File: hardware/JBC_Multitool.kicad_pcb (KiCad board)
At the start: 2 copper layers, 122 x 93 mm, 46 parts, among them J1 Screw_Terminal_01x02, J4 Mini XLR6, J5 Mini XLR6, J6 Binder 09-0998-00-05, J7 Binder 09-0998-00-05, K1 RT314005, K10 HF49FD_005-1H12T, K11 HF49FD_005-1H12T, K2 HF49FD_005-1H12T, K3 HF49FD_005-1H12T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

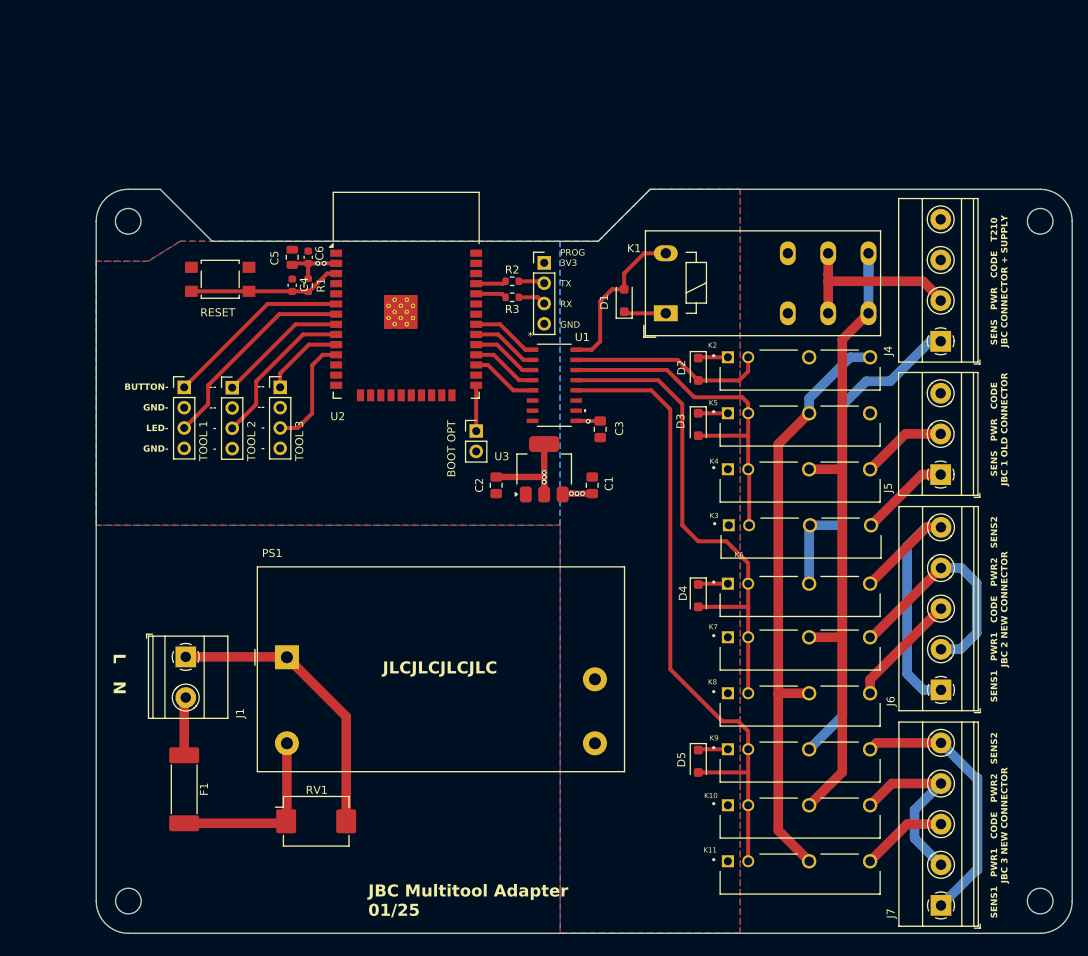
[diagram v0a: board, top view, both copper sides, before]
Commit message: corrected pin numbers on terminal footprint, changed switch-LED configuration
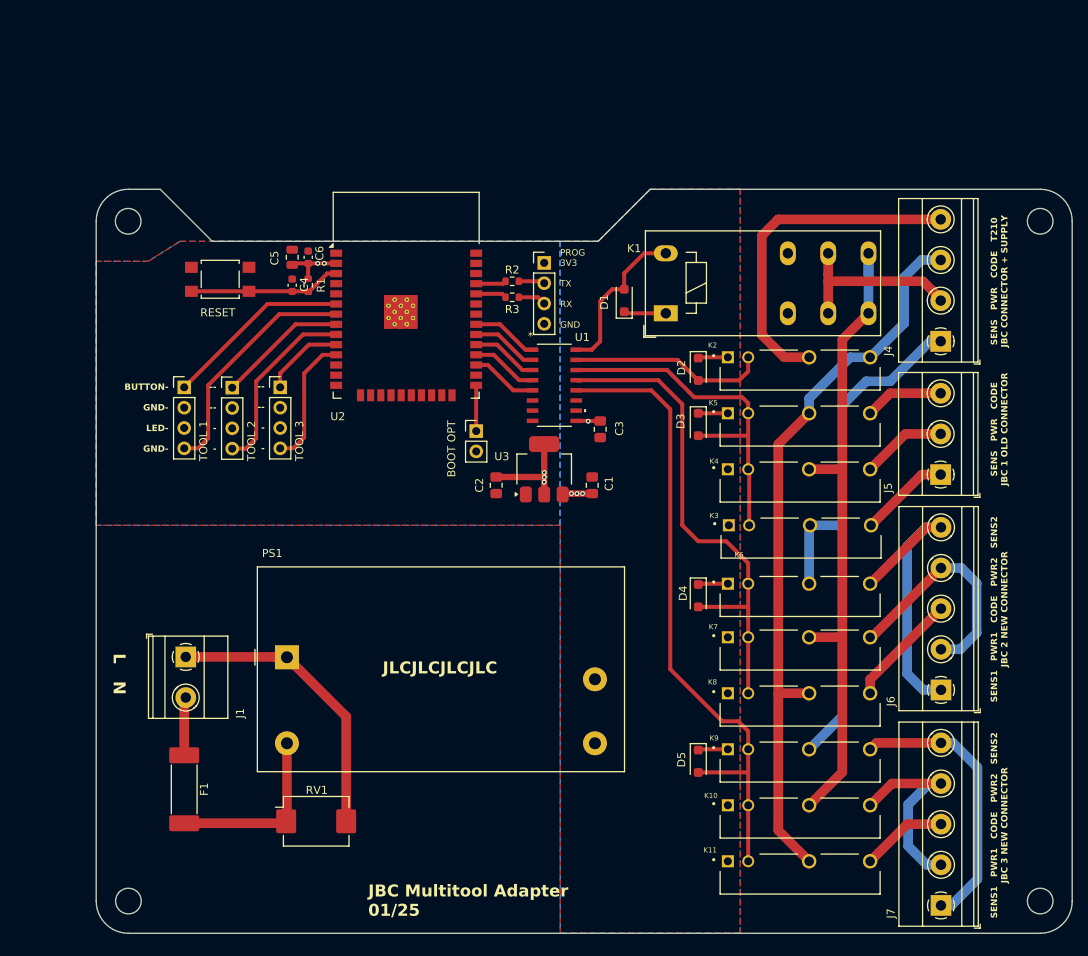
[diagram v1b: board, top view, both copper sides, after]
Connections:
- SELECT_TOOL_1 pad 3: /SELECT_TOOL_LED_1 -> +3.3V
- SELECT_TOOL_1 pad 4: GND -> /SELECT_TOOL_LED_1
- SELECT_TOOL_2 pad 3: /SELECT_TOOL_LED_2 -> +3.3V
- SELECT_TOOL_2 pad 4: GND -> /SELECT_TOOL_LED_2
- SELECT_TOOL_3 pad 3: /SELECT_TOOL_LED_3 -> +3.3V
- SELECT_TOOL_3 pad 4: GND -> /SELECT_TOOL_LED_3
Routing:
- net /RELAIS_CARD/T210_TOOL_CODE: track 0.00 -> 42.7 mm
- net /RELAIS_CARD/TOOL_CODE: track 74.7 -> 91.9 mm
- net Net-(J5-P5): track 0.00 -> 9.86 mm
- net /SELECT_TOOL_LED_1: track 26.3 -> 29.8 mm
- net /SELECT_TOOL_LED_2: track 19.5 -> 23.1 mm
- net Net-(J7-P2): track 23.7 -> 26.2 mm
- net /SELECT_TOOL_LED_3: track 14.3 -> 16.5 mm
- net Net-(J7-P1): track 33.5 -> 34.9 mm

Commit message: added 2.nd "old" jbc connector
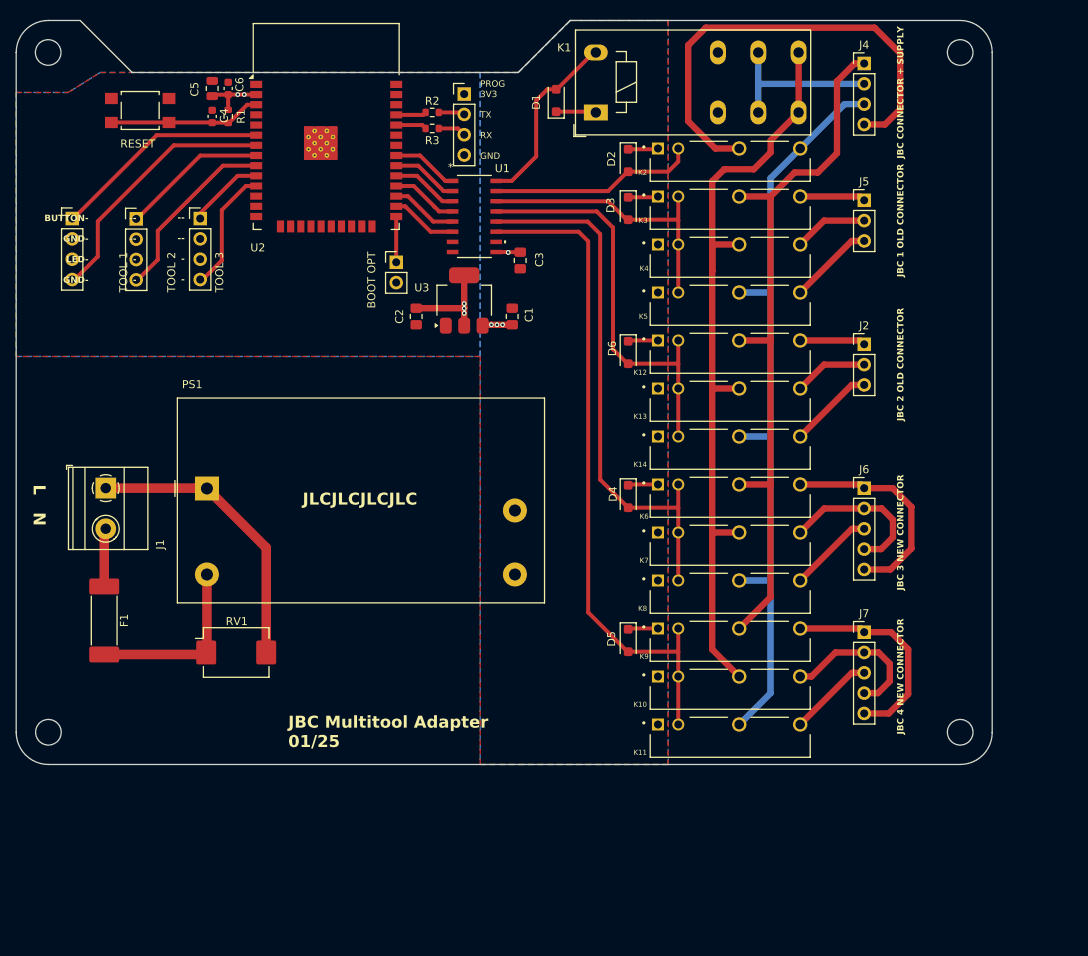
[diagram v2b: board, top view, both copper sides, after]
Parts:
- added D6: D, Diode_SMD:D_SOD-123F, F.Cu at (148.5, 85.4)
- added J2: Mini XLR6, Connector_PinHeader_2.54mm:PinHeader_1x03_P2.54mm_Vertical, F.Cu at (178.0, 84.4)
- added K12: HF49FD_005-1H12T, HF49FD:HF49FD, F.Cu at (161.2, 85.5)
- added K13: HF49FD_005-1H12T, HF49FD:HF49FD, F.Cu at (161.2, 91.5)
- added K14: HF49FD_005-1H12T, HF49FD:HF49FD, F.Cu at (161.2, 97.5)
- J4: footprint TerminalBlock_Phoenix:TerminalBlock_Phoenix_MKDS-1,5-4-5.08_1x04_P5.08mm_Horizontal -> Connector_PinHeader_2.54mm:PinHeader_1x04_P2.54mm_Vertical
- J5: footprint TerminalBlock_Phoenix:TerminalBlock_Phoenix_MKDS-1,5-3-5.08_1x03_P5.08mm_Horizontal -> Connector_PinHeader_2.54mm:PinHeader_1x03_P2.54mm_Vertical
- J6, J7: footprint TerminalBlock_Phoenix:TerminalBlock_Phoenix_MKDS-1,5-5-5.08_1x05_P5.08mm_Horizontal -> Connector_PinHeader_2.54mm:PinHeader_1x05_P2.54mm_Vertical
- moved K3 42.0 mm to (161.2, 67.5)
- moved J4 36.0 mm to (178.0, 49.3), turned to 0 degrees
- moved J5 35.6 mm to (178.0, 66.4), turned to 0 degrees
- moved J7 35.5 mm to (178.0, 120.4), turned to 0 degrees
- moved K4 29.4 mm to (161.2, 73.5)
- moved D3 28.4 mm to (148.5, 67.4)
- moved D2 27.5 mm to (148.5, 61.4)
- moved K2 27.5 mm to (161.2, 61.5)
- moved J6 27.0 mm to (178.0, 102.4), turned to 0 degrees
- moved K1 26.6 mm to (144.5, 55.4)
- moved D1 26.4 mm to (139.5, 53.9)
- moved SELECT_TOOL_1 25.3 mm to (79.0, 68.7)
- moved SELECT_TOOL_2 24.3 mm to (87.0, 68.7)
- moved SELECT_TOOL_3 23.3 mm to (95.0, 68.7)
- moved C4 23.3 mm to (96.5, 55.9)
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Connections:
- D4 pad 2: /RELAIS_CARD/TOOL_2_SEL -> /RELAIS_CARD/TOOL_3_SEL
- D5 pad 2: /RELAIS_CARD/TOOL_3_SEL -> /RELAIS_CARD/TOOL_4_SEL
- K10 pad 2: /RELAIS_CARD/TOOL_3_SEL -> /RELAIS_CARD/TOOL_4_SEL
- K11 pad 2: /RELAIS_CARD/TOOL_3_SEL -> /RELAIS_CARD/TOOL_4_SEL
- K6 pad 2: /RELAIS_CARD/TOOL_2_SEL -> /RELAIS_CARD/TOOL_3_SEL
- K7 pad 2: /RELAIS_CARD/TOOL_2_SEL -> /RELAIS_CARD/TOOL_3_SEL
- K8 pad 2: /RELAIS_CARD/TOOL_2_SEL -> /RELAIS_CARD/TOOL_3_SEL
- K9 pad 2: /RELAIS_CARD/TOOL_3_SEL -> /RELAIS_CARD/TOOL_4_SEL
- U1 pad 11: unconnected-(U1-OUT6-Pad11) -> /RELAIS_CARD/TOOL_4_SEL
- U1 pad 6: unconnected-(U1-IN6-Pad6) -> /TOOL_4_CTRL
- U2 pad 26: unconnected-(U2-IO4-Pad26) -> /TOOL_4_CTRL
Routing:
- net /RELAIS_CARD/TOOL_4_SEL: track 0.00 -> 83.7 mm
- net /RELAIS_CARD/TOOL_SENSOR: track 71.8 -> 91.3 mm
- net /RELAIS_CARD/TOOL_POWER: track 83.8 -> 99.6 mm
- net /RELAIS_CARD/T210_TOOL_CODE: track 42.7 -> 58.3 mm
- net /RELAIS_CARD/TOOL_3_SEL: track 80.7 -> 67.6 mm
- net /RELAIS_CARD/TOOL_2_SEL: track 62.6 -> 51.5 mm
- net Net-(J6-P1): track 38.0 -> 27.2 mm
- net Net-(J2-P5): track 0.00 -> 10.7 mm
- net Net-(J6-P2): track 29.2 -> 19.8 mm
- net Net-(J2-P2): track 0.00 -> 9.24 mm
- net /RELAIS_CARD/TOOL_1_SEL: track 44.6 -> 35.8 mm
- net /TOOL_4_CTRL: track 0.00 -> 8.37 mm
- net Net-(J7-P1): track 34.9 -> 26.7 mm
- net Net-(J2-P1): track 0.00 -> 8.20 mm
- net Net-(J7-P2): track 26.2 -> 19.0 mm
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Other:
- board text added: "JBC 1 OLD CONNECTOR"
- board text added: "JBC 2 OLD CONNECTOR"
- board text added: "JBC 3 NEW CONNECTOR"
- board text added: "JBC 4 NEW CONNECTOR"
- board text added: "JBC CONNECTOR + SUPPLY"
- board text removed: "SENS PWR CODE JBC 1 OLD CONNECTOR"
- board text removed: "SENS PWR CODE T210 JBC CONNECTOR + SUPPLY"
- board text removed: "SENS1 PWR1 CODE PWR2 SENS2 JBC 2 NEW CONNECTOR"
- board text removed: "SENS1 PWR1 CODE PWR2 SENS2 JBC 3 NEW CONNECTOR"

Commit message: changed pcb front silkscreen
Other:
- board text added: "JBC CONNECTOR MAIN"
- board text added: "JBC TOOL 1 (OLD)"
- board text added: "JBC TOOL 2 (OLD)"
- board text added: "JBC TOOL 3 (NEW)"
- board text added: "JBC TOOL 4 (NEW)"
- board text removed: "JBC 1 OLD CONNECTOR"
- board text removed: "JBC 2 OLD CONNECTOR"
- board text removed: "JBC 3 NEW CONNECTOR"
- board text removed: "JBC 4 NEW CONNECTOR"
- board text removed: "JBC CONNECTOR + SUPPLY"
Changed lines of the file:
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@@
 		)
 	)
-	(gr_text "JBC CONNECTOR + SUPPLY"
+	(gr_text "JBC CONNECTOR MAIN"
 		(at 183 52.9 90)
 		(layer "F.SilkS")
@@
 		)
 	)
-	(gr_text "JBC 3 NEW CONNECTOR"
+	(gr_text "JBC TOOL 3 (NEW)"
 		(at 183 107.9 90)
 		(layer "F.SilkS")
@@
 		)
 	)
-	(gr_text "JBC 1 OLD CONNECTOR"
-		(at 183 68.9 90)
+	(gr_text "JBC TOOL 1 (OLD)"
+		(at 183 69 90)
 		(layer "F.SilkS")
 		(effects
@@
 		)
 	)
-	(gr_text "JBC 2 OLD CONNECTOR"
+	(gr_text "JBC TOOL 2 (OLD)"
 		(at 183 86.9 90)
 		(layer "F.SilkS")
@@
 		)
 	)
-	(gr_text "JBC 4 NEW CONNECTOR"
+	(gr_text "JBC TOOL 4 (NEW)"
 		(at 183 125.9 90)
 		(layer "F.SilkS")

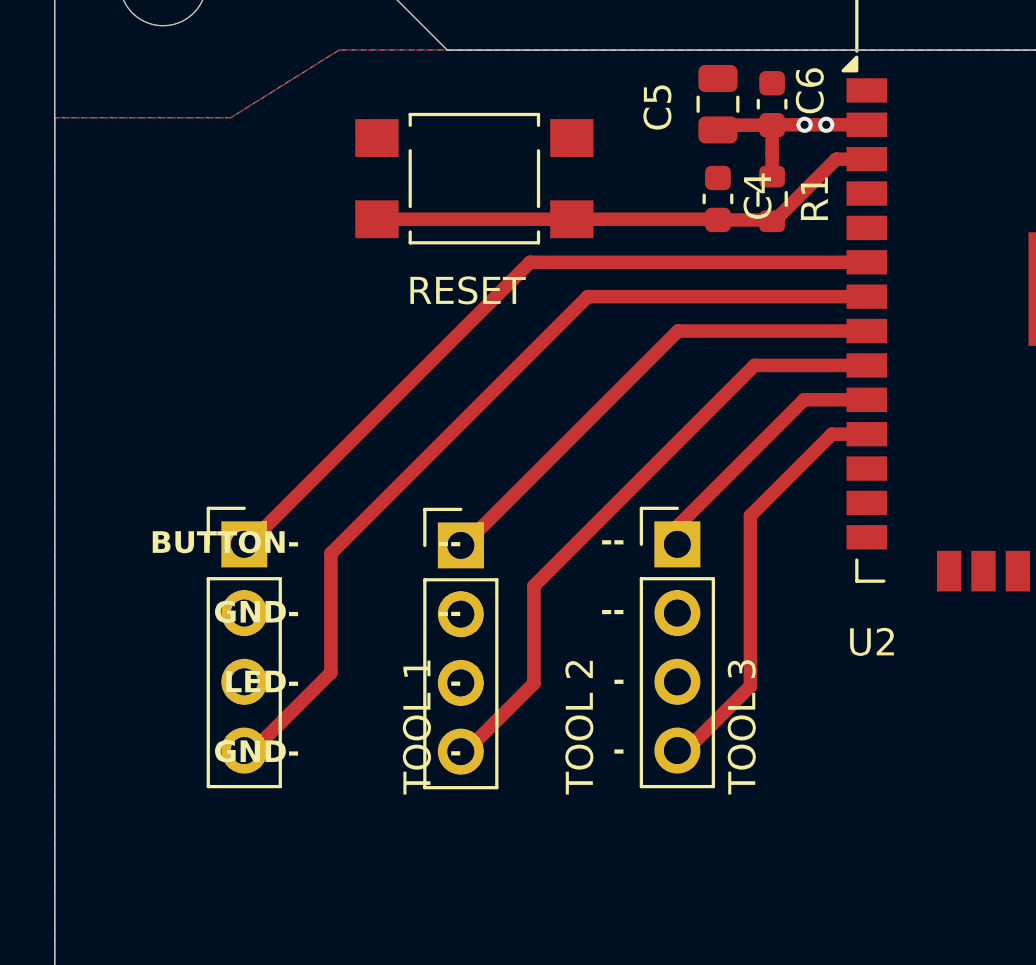
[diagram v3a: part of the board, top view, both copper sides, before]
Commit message: added tool change switch 4
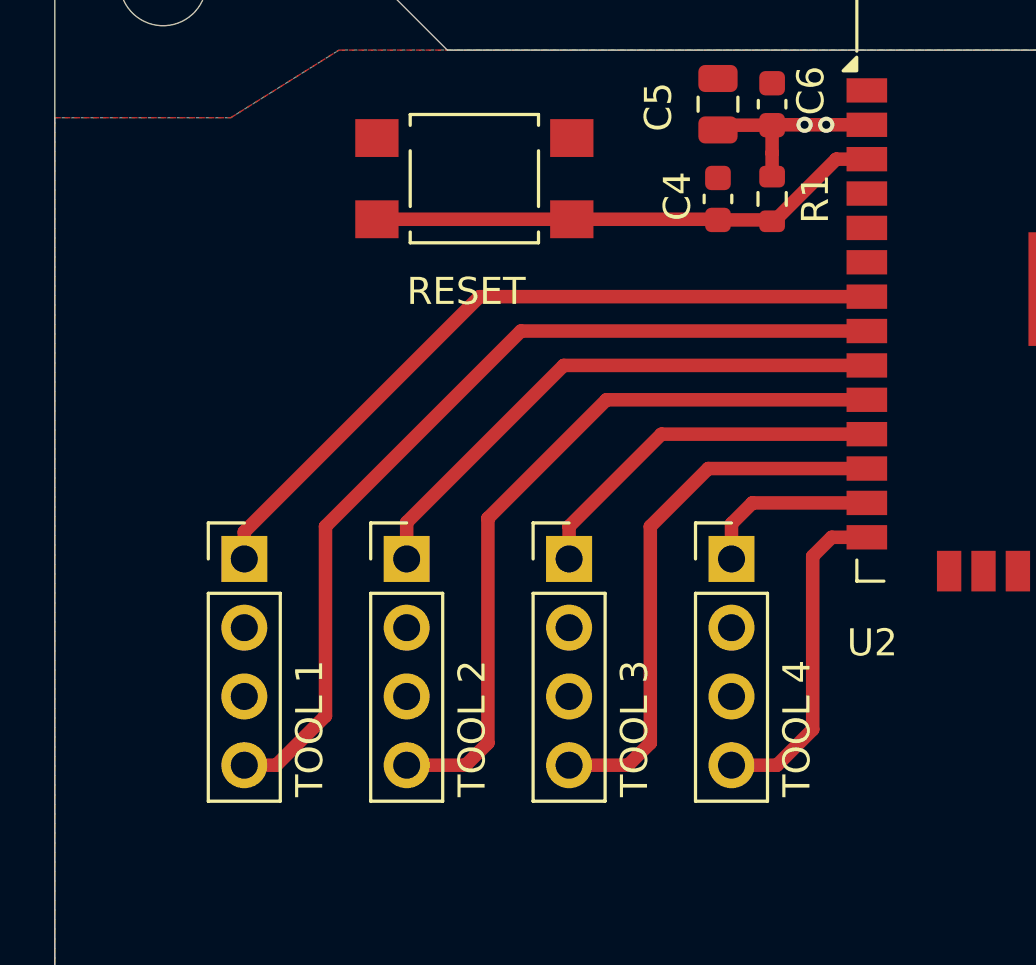
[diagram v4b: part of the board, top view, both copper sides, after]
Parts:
- added SELECT_TOOL_4: Conn_01x04, Connector_PinHeader_2.54mm:PinHeader_1x04_P2.54mm_Vertical, F.Cu at (97.0, 69.2)
- moved SELECT_TOOL_3 4.04 mm to (91.0, 69.2)
- moved SELECT_TOOL_2 2.06 mm to (85.0, 69.2)
- moved SELECT_TOOL_1 0.54 mm to (79.0, 69.2)
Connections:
- U2 pad 10: /SELECT_TOOL_3 -> /SELECT_TOOL_LED_2
- U2 pad 11: /SELECT_TOOL_LED_3 -> /SELECT_TOOL_3
- U2 pad 12: unconnected-(U2-IO27-Pad12) -> /SELECT_TOOL_LED_3
- U2 pad 13: unconnected-(U2-IO14-Pad13) -> /SELECT_TOOL_4
- U2 pad 14: unconnected-(U2-IO12-Pad14) -> /SELECT_TOOL_LED_4
- U2 pad 6: /SELECT_TOOL_1 -> unconnected-(U2-IO34-Pad6)
- U2 pad 7: /SELECT_TOOL_LED_1 -> /SELECT_TOOL_1
- U2 pad 8: /SELECT_TOOL_2 -> /SELECT_TOOL_LED_1
- U2 pad 9: /SELECT_TOOL_LED_2 -> /SELECT_TOOL_2
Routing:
- net /SELECT_TOOL_LED_4: track 0.00 -> 12.2 mm
- net /SELECT_TOOL_4: track 0.00 -> 6.62 mm
- net /SELECT_TOOL_LED_3: track 15.5 -> 20.2 mm
- net /SELECT_TOOL_LED_2: track 23.0 -> 27.5 mm
- net /SELECT_TOOL_3: track 9.60 -> 13.6 mm
- net /SELECT_TOOL_2: track 18.3 -> 20.8 mm
- net /SELECT_TOOL_LED_1: track 32.5 -> 33.7 mm
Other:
- board text added: "TOOL 4"
- board text removed: "-- -- - -"
- board text removed: "BUTTON- GND- LED- GND-"

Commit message: add gerber and bom
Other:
- board text added: "-- -- - -"
- board text added: "BTTN- GND- LED- GND-"

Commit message: fix pcb
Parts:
- moved R3 0.85 mm to (124.0, 58.2)
- moved R2 0.35 mm to (124.0, 55.8)
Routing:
- net /RELAIS_CARD/T210_TOOL_CODE: track 58.3 -> 44.8 mm
- net /RELAIS_CARD/TOOL_SENSOR: track 91.3 -> 85.1 mm
- net /RELAIS_CARD/TOOL_CODE: track 97.3 -> 92.3 mm
- net /RELAIS_CARD/TOOL_POWER: track 99.6 -> 95.5 mm
- net /RELAIS_CARD/TOOL_POWER_SEL: track 23.4 -> 25.7 mm
- net Net-(J1-Pin_1): track 36.3 -> 38.2 mm
- net Net-(J6-P1): track 27.2 -> 25.5 mm
- net Net-(J7-P1): track 26.7 -> 25.8 mm
